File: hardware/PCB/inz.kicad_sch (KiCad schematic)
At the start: 24 parts, among them J1 Conn_01x20_Socket, J10 WCS1800, J11 INA333, J12 Micro SD Adapter, J13 Relays, J2 Conn_01x20_Socket, J3 USB_C_Receptacle_USB2.0_16P, J4 Barrel_Jack_Switch, J5 J_OLED, J6 J_SGP30, J7 J_BMP1, J8 J_BMP2, J9 J_BMP3, U1 LM2596S-ADJ, U3 USBLC6-2SC6

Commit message: pcb
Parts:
- removed J10: WCS1800, Connector_PinHeader_2.54mm:PinHeader_1x04_P2.54mm_Vertical, symbol Connector:Conn_01x04_Pin
- removed J11: INA333, Connector_PinHeader_2.54mm:PinHeader_1x04_P2.54mm_Vertical, symbol Connector:Conn_01x04_Pin
- removed J12: Micro SD Adapter, Connector_PinHeader_2.54mm:PinHeader_1x06_P2.54mm_Vertical, symbol Connector:Conn_01x06_Pin
- removed J13: Relays, Connector_PinHeader_2.54mm:PinHeader_1x06_P2.54mm_Vertical, symbol Connector:Conn_01x06_Pin
- removed J4: Barrel_Jack_Switch, Connector_BarrelJack:BarrelJack_Horizontal, symbol Connector:Barrel_Jack_Switch
- added C104, C105, C106: 100n, Capacitor_SMD:C_0805_2012Metric, symbol Device:C
- added D101: D_Schottky, Diode_SMD:D_SMA, symbol Device:D_Schottky
- added F201: 2A, Fuse:Fuseholder_Clip-5x20mm_Littelfuse_111_Inline_P20.00x5.00mm_D1.05mm_Horizontal, symbol Device:Polyfuse
- added J102: Conn_01x02, symbol Connector_Generic:Conn_01x02
- added J103: enc, Connector_PinHeader_2.54mm:PinHeader_1x05_P2.54mm_Vertical, symbol Connector:Conn_01x05_Pin
- added R104, R105, R106: 5.1k, Resistor_SMD:R_0805_2012Metric, symbol Device:R
- added SW101: RotaryEncoder_Switch_MP, symbol Device:RotaryEncoder_Switch_MP
- J5: now left out of the parts list
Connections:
- net 5V is gone; now on net +5V: J1.18 (Pin_18)
- net +3V3: now also J103.1 (Pin_1); no longer J1.20 (Pin_20), J2.3 (Pin_3)
- net BMP1_CS: no longer J1.11 (Pin_11), J2.11 (Pin_11), J8.5 (Pin_5)
- net GND: now also C104.2, C105.2, C106.2, J103.5 (Pin_5), SW101.S2
- net +5V: now reaches Cin.1, U1.1 (VIN)
- net +5V: now also J2.1 (Pin_1)
- net B0 renamed QNH_out_B0
- net B1 renamed ina333_Vout_B1
- net VUSB: no longer names the net of J3.A4 (VBUS), J3.A9 (VBUS), J3.B4 (VBUS), J3.B9 (VBUS), U3.5 (VBUS)
- new net 3V3: J1.20 (Pin_20), J2.3 (Pin_3)
- new net B3: J1.11 (Pin_11), J8.5 (Pin_5)
- new net SD_CS: J2.11 (Pin_11)
- new net Sensors1/ina333_Vin+: J102.1 (Pin_1)
- new net Sensors1/ina333_Vin-: J102.2 (Pin_2)
- new net enc_KEY: C106.1, R106.2
- new net enc_S1: C104.1, R104.2
- new net enc_S1_in: J103.4 (Pin_4), R104.1
- new net enc_S2: C105.1, R105.2
- new net enc_S2_in: J103.3 (Pin_3), R105.1
- new net enc_key_in: J103.2 (Pin_2), R106.1, SW101.S1
- no-connect marks 9 -> 3
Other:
- added sheet Sensors1 (Sensors1.kicad_sch)
- note added: "Botland footprint"
- note added: "D"
- note added: "JST-XH 2.5mm"
- note added: "VCC GND SCK MOSI CS MISO"
- note added: "dupont 2.54mm"
- note added: "globalne na lokalne"
- note added: "kolejnosc"
- note added: "to ja zrobie"
- note added: "to zmienic na 2.8 pinout"
- note added: "wszędzie maja byc miejsca na zamontowanie przewodów zewnetrznych BMS TP4056 - footprint"
- note removed: "Tutaj chyba mial byc jakis modul na obudowe do wsadzania a reszta jakies rezystorki cos to na pcb?"
- note removed: "chyba sie zesra jak 3.3v i 5v na raz podlacze?"
- moved on the sheet: J1, J2, J3, J5, J6, J7, J8, J9, R3, R4, U3

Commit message: pcb commit
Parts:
- removed J5: J_OLED, Connector_PinHeader_2.54mm:PinHeader_1x08_P2.54mm_Vertical, symbol Connector:Conn_01x08_Pin
- removed J6: J_SGP30, Connector_PinHeader_2.54mm:PinHeader_1x05_P2.54mm_Vertical, symbol Connector:Conn_01x05_Pin
- added C2: 10u, Capacitor_SMD:C_0805_2012Metric, symbol Device:C
- added J4: J_OLED, Connector_PinHeader_2.54mm:PinHeader_1x14_P2.54mm_Vertical, symbol Connector:Conn_01x14_Pin
- added J5: J_SGP30, symbol Connector:Conn_01x04_Pin
- added J_BAT1: Conn_01x02, TerminalBlock:TerminalBlock_MaiXu_MX126-5.0-02P_1x02_P5.00mm, symbol Connector_Generic:Conn_01x02
- added Q2: IRLZ44N, Package_TO_SOT_THT:TO-220-3_Vertical, symbol Transistor_FET:IRLZ44N
- added R5: 1k, Resistor_SMD:R_0805_2012Metric, symbol Device:R
- added R6: 1, Resistor_SMD:R_0805_2012Metric, symbol Device:R
- added U4: LM358, footprints:LM358, symbol Amplifier_Operational:LM358
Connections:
- net +3V3: now also J4.1 (Pin_1), J4.8 (Pin_8), J5.1 (Pin_1)
- net +5V: now also U4.8 (V+)
- net GND: now also C2.2, J4.2 (Pin_2), J5.2 (Pin_2), J_BAT1.2 (Pin_2), R6.1, U4.4 (V-)
- net B3 renamed BMP2_CS
- net BMP2_CS: no longer J1.11 (Pin_11)
- net B4 renamed TIM3_CH1_PWM_B4
- net TIM3_CH1_PWM_B4: now also R5.1
- removed net BMP1_CS: J1.13 (Pin_13), J1.16 (Pin_16), J2.14 (Pin_14), J7.5 (Pin_5), J9.5 (Pin_5)
- net I2C_SCL renamed I2C_SCL_B6
- net I2C_SCL_B6: now also J5.3 (Pin_3)
- net I2C_SDA renamed I2C_SDA_B9
- net I2C_SDA_B9: now also J5.4 (Pin_4)
- net OLED_DC renamed OLED_DC_A2
- net OLED_DC_A2: now also J4.5 (Pin_5)
- net OLED_RST renamed OLED_RST_A3
- net OLED_RST_A3: now also J4.4 (Pin_4)
- net R1IN1 renamed R1_IN1_B12
- net R1IN2 renamed R1_IN2_B13
- net R1IN3 renamed R1_IN3_B14
- net SD_CS renamed SD_CS_A4
- net SPI_MISO renamed SPI_MISO_A6
- net SPI_MISO_A6: now also J4.9 (Pin_9)
- net SPI_MOSI renamed SPI_MOSI_A7
- net SPI_MOSI_A7: now also J4.6 (Pin_6)
- net SPI_SCK renamed SPI_SCK_A5
- net SPI_SCK_A5: now also J4.7 (Pin_7)
- net USB_D+ renamed USB_D+_A12
- net USB_D- renamed USB_D-_A11
- new net: C2.1, R5.2, U4.3 (+)
- new net: J_BAT1.1 (Pin_1), Q2.2 (D)
- new net: Q2.1 (G), U4.1
- new net: Q2.3 (S), R6.2, U4.2 (-)
- new net BMP1_CS_B5: J1.13 (Pin_13), J7.5 (Pin_5)
- new net BMP2_CS_B3: J1.11 (Pin_11)
- new net BMP3_CS_B8: J1.16 (Pin_16), J9.5 (Pin_5)
- new net OLED_CS_A1: J2.14 (Pin_14), J4.3 (Pin_3)
- no-connect marks 3 -> 7
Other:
- note added: "Bat+"
- note added: "Bat-"
- note added: "VCC GND CS RESET DC/RS SDI(MOSI) SCK LED SDO(MISO) T_CLK T_CS T_DIN T_DO T_IRQ"
- note added: "VCC GND SCL SDA"
- note added: "https://piotr-gorecki.pl/yk012-wspolnie-projektujemy-uniwersalne-obciazenie-aktywne/"
- note added: "lm358 irlz44n 10uF R = 1kohm ? Rs = 1ohm"
- note removed: "globalne na lokalne"
- note removed: "kolejnosc"
- note removed: "to zmienic na 2.8 pinout"
- moved on the sheet: C104, C105, C106, J103, J3, R104, R105, R106, R3, R4, SW101, U3

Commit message: PCB
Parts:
- removed C2: 10u, Capacitor_SMD:C_0805_2012Metric, symbol Device:C
- removed Cf: 2.2n, Capacitor_SMD:C_0805_2012Metric, symbol Device:C
- removed Cin: 150uF, Capacitor_SMD:CP_Elec_8x10.5, symbol Device:C_Polarized
- removed Cout: 680uF, Capacitor_SMD:CP_Elec_16x17.5, symbol Device:C_Polarized
- removed D1: 650mV 3A, Diode_SMD:D_SMA, symbol Device:D_Schottky
- removed J4: J_OLED, Connector_PinHeader_2.54mm:PinHeader_1x14_P2.54mm_Vertical, symbol Connector:Conn_01x14_Pin
- removed J5: J_SGP30, symbol Connector:Conn_01x04_Pin
- removed J7: J_BMP1, Connector_PinHeader_2.54mm:PinHeader_1x06_P2.54mm_Vertical, symbol Connector:Conn_01x06_Pin
- removed J8: J_BMP2, Connector_PinHeader_2.54mm:PinHeader_1x06_P2.54mm_Vertical, symbol Connector:Conn_01x06_Pin
- removed J9: J_BMP3, Connector_PinHeader_2.54mm:PinHeader_1x06_P2.54mm_Vertical, symbol Connector:Conn_01x06_Pin
- removed J_BAT1: Conn_01x02, TerminalBlock:TerminalBlock_MaiXu_MX126-5.0-02P_1x02_P5.00mm, symbol Connector_Generic:Conn_01x02
- removed L1: 39uH, Inductor_SMD:L_12x12mm_H8mm, symbol Device:L
- removed Q2: IRLZ44N, Package_TO_SOT_THT:TO-220-3_Vertical, symbol Transistor_FET:IRLZ44N
- removed R5: 1k, Resistor_SMD:R_0805_2012Metric, symbol Device:R
- removed R6: 1, Resistor_SMD:R_0805_2012Metric, symbol Device:R
- removed Rfb1: 3.3k, Resistor_SMD:R_0805_2012Metric, symbol Device:R
- removed Rfb2: 5.6k, Resistor_SMD:R_0805_2012Metric, symbol Device:R
- removed U1: LM2596S-ADJ, Package_TO_SOT_SMD:TO-263-5_TabPin3, symbol Regulator_Switching:LM2596S-ADJ
- removed U4: LM358, footprints:LM358, symbol Amplifier_Operational:LM358
- added C107, C109, C110: 100n, Capacitor_SMD:C_0805_2012Metric, symbol Device:C
- added C108: 2.2u, Capacitor_SMD:C_0805_2012Metric, symbol Device:C
- added L101: 2.2uH, Inductor_SMD:L_Sunlord_MWSA0503S, symbol Device:L
- added R107: 100k, Resistor_SMD:R_0805_2012Metric, symbol Device:R
- added R108: 22.1k, Resistor_SMD:R_0805_2012Metric, symbol Device:R
- added U101: LMR51430, Package_TO_SOT_SMD:SOT-23-6, symbol Regulator_Switching:LMR51430
- C104, C105, C106: Distributor https://jlcpcb.com/partdetail/28983-CL21B104KCFNNNE/C28233 -> (none); JLCPCB Part (none) -> C28233; Link (none) -> https://jlcpcb.com/partdetail/28983-CL21B104KCFNNNE/C28233
- D101: value D_Schottky -> D_Schottky_3A; Distributor https://jlcpcb.com/partdetail/MDD_Microdiode_Semiconductor-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 -> (none); JLCPCB Part (none) -> C8678; Link (none) -> https://jlcpcb.com/partdetail/MDD_Microdiode_Semiconductor-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
- F201: value 2A -> xA; Distributor https://jlcpcb.com/partdetail/XuchengElec-5x20/C3130 -> (none); Link (none) -> https://jlcpcb.com/partdetail/XuchengElec-5x20/C3130; MFR Part 5x20 环保 保险管夹/座 -> (none); Manufacturer Xucheng Elec -> (none); now left out of the parts list
- J102: value Conn_01x02 -> ina333; footprint (none) -> TerminalBlock:TerminalBlock_MaiXu_MX126-5.0-02P_1x02_P5.00mm
- J103: JLCPCB Part (none) -> C2337; LCSC C2337 -> (none)
- J3: Link (none) -> https://jlcpcb.com/partdetail/3554049-USB4105_GF_A060/C3025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; Link 1 https://jlcpcb.com/partdetail/3554049-USB4105_GF_A060/C3025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 -> (none)
- R104, R105, R106: Distributor https://jlcpcb.com/partdetail/28584-0805W8F5101T5E/C27834 -> (none); Link (none) -> https://jlcpcb.com/partdetail/28584-0805W8F5101T5E/C27834
- R3, R4: footprint (none) -> Resistor_SMD:R_0805_2012Metric; Link (none) -> https://jlcpcb.com/partdetail/28584-0805W8F5101T5E/C27834; MFR Part (none) -> 0805W8F5101T5E; Manufacturer (none) -> UNI-ROYAL(Uniroyal Elec)
- U3: Likn 1 https://jlcpcb.com/partdetail/STMicroelectronics-USBLC62SC6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 -> (none); Link (none) -> https://jlcpcb.com/partdetail/STMicroelectronics-USBLC62SC6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
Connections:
- net +5V is gone; now on net VBUS: J1.18 (Pin_18), J2.1 (Pin_1)
- net +3V3: now also C110.2, L101.2, R107.1
- net GND: now also C108.2, C109.2, C110.1, R108.2, U101.1 (GND)
- net at D101.1 (K): now also F201.1
- net VBUS: now reaches D101.2 (A)
- net at F201.2: now also C108.1, C109.1, U101.3 (VIN), U101.5 (EN)
- new net: C107.1, L101.1, U101.2 (SW)
- new net: R107.2, R108.1, U101.4 (FB)
- new net: C107.2, U101.6 (CB)
- no-connect marks 7 -> 2
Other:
- added sheet Connectors (Connectors.kicad_sch)
- added sheet Sensors2 (Sensors2.kicad_sch)
- sheet Sensors1 ports: added pwm_current_sel; removed none
- note added: "5.0V -> 3.3V"
- note removed: "Bat+"
- note removed: "Bat-"
- note removed: "D"
- note removed: "JST-XH 2.5mm"
- note removed: "VCC GND CS RESET DC/RS SDI(MOSI) SCK LED SDO(MISO) T_CLK T_CS T_DIN T_DO T_IRQ"
- note removed: "VCC GND SCK MOSI CS MISO"
- note removed: "VCC GND SCL SDA"
- note removed: "dupont 2.54mm"
- note removed: "https://piotr-gorecki.pl/yk012-wspolnie-projektujemy-uniwersalne-obciazenie-aktywne/"
- note removed: "lm358 irlz44n 10uF R = 1kohm ? Rs = 1ohm"
- note removed: "to ja zrobie"
- moved on the sheet: D101, F201

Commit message: PCB
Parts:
- removed J1, J2: Conn_01x20_Socket, symbol Connector:Conn_01x20_Socket
- removed SW101: RotaryEncoder_Switch_MP, symbol Device:RotaryEncoder_Switch_MP
- added J15: STM32blackpill, footprints:STM32blackpill, symbol footprints:STM32blackpill
- added JP2: SolderJumper_2_Open, Jumper:SolderJumper-2_P1.3mm_Open_TrianglePad1.0x1.5mm, symbol Jumper:SolderJumper_2_Open
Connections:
- net GND: now also J15.19 (GND), J15.22 (GND)
- net +5V: now reaches C108.1, C109.1, F201.2, U101.3 (VIN), U101.5 (EN)
- net +5V: now also J15.18 (5V), J15.21 (5V)
- net USB_D+_A12 renamed USB_D+
- net USB_D+: now also J15.9 (PA12)
- net USB_D-_A11 renamed USB_D-
- net USB_D-: now also J15.8 (PA11)
- new net BMP1_CS: J15.13 (PB5)
- new net BMP2_CS: J15.11 (PB3)
- new net BMP3_CS: J15.16 (PB8)
- new net I2C_SCL: J15.14 (PB6)
- new net I2C_SDA: J15.17 (PB9)
- new net OLED_CS: J15.34 (PA1)
- new net OLED_DC: J15.33 (PA2)
- new net OLED_RST: J15.32 (PA3)
- new net QNH_out: J15.27 (PB0)
- new net R1_IN1: J15.1 (PB12)
- new net R1_IN2: J15.2 (PB13)
- new net R1_IN3: J15.3 (PB14)
- new net SD_CS: J15.31 (PA4)
- new net SPI_MISO: J15.29 (PA6)
- new net SPI_MOSI: J15.28 (PA7)
- new net SPI_SCK: J15.30 (PA5)
- new net Sensors1/Current_sensor_in+: JP2.1 (A)
- new net Sensors1/Current_sensor_in-: JP2.2 (B)
- new net TIM3_CH1_PWM: J15.12 (PB4)
- new net ina333_Vout: J15.26 (PB1)
- no-connect marks 2 -> 5
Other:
- sheet Sensors1 ports: added BME280_SPI_CLK, BME280_SPI_MISO, BME282_SPI_MOSI, BME283_SPI_CS, Current_sensor_in+, Current_sensor_in-; removed pwm_current_sel
- sheet Sensors2 ports: added pwm_current_sel; removed none
- note removed: "Botland footprint"
- moved on the sheet: J102

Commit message: pcb sensors
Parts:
- removed C104, C105, C106, C107, C109, C110: 100n, Capacitor_SMD:C_0805_2012Metric, symbol Device:C
- removed C108: 2.2u, Capacitor_SMD:C_0805_2012Metric, symbol Device:C
- removed D101: D_Schottky_3A, Diode_SMD:D_SMA, symbol Device:D_Schottky
- removed F201: xA, Fuse:Fuseholder_Clip-5x20mm_Littelfuse_111_Inline_P20.00x5.00mm_D1.05mm_Horizontal, symbol Device:Polyfuse
- removed J102: ina333, TerminalBlock:TerminalBlock_MaiXu_MX126-5.0-02P_1x02_P5.00mm, symbol Connector_Generic:Conn_01x02
- removed J103: enc, Connector_PinHeader_2.54mm:PinHeader_1x05_P2.54mm_Vertical, symbol Connector:Conn_01x05_Pin
- removed J3: USB_C_Receptacle_USB2.0_16P, Connector_USB:USB_C_Receptacle_GCT_USB4105-xx-A_16P_TopMnt_Horizontal, symbol Connector:USB_C_Receptacle_USB2.0_16P
- removed L101: 2.2uH, Inductor_SMD:L_Sunlord_MWSA0503S, symbol Device:L
- removed R104, R105, R106, R3, R4: 5.1k, Resistor_SMD:R_0805_2012Metric, symbol Device:R
- removed R107: 100k, Resistor_SMD:R_0805_2012Metric, symbol Device:R
- removed R108: 22.1k, Resistor_SMD:R_0805_2012Metric, symbol Device:R
- removed U101: LMR51430, Package_TO_SOT_SMD:SOT-23-6, symbol Regulator_Switching:LMR51430
- removed U3: USBLC6-2SC6, Package_TO_SOT_SMD:SOT-23-6, symbol Power_Protection:USBLC6-2SC6
- added J101: battery cell, symbol Connector:Screw_Terminal_01x02
- added U105: TP4056, symbol footprints:TP4056
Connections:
- net GND: now also U105.2 (GND), U105.6 (OUT-)
- net enc_KEY: now also J15.7 (PA10)
- net enc_S1: now also J15.5 (PA8)
- net enc_S2: now also J15.6 (PA9)
- net Sensors1/Current_sensor_in+ renamed Current_sensor_in+
- net Current_sensor_in+: now also J101.2 (Pin_2)
- net Sensors1/Current_sensor_in- renamed Current_sensor_in-
- net Current_sensor_in-: now also U105.4 (BAT+)
- new net K1_NO: U105.1 (Vusb)
- new net K2_COM: U105.3 (OUT+)
- new net ina333_Vin-: J101.1 (Pin_1), U105.5 (BAT-)
- no-connect marks 5 -> 3
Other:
- added sheet Relays (Relays.kicad_sch)
- sheet Connectors ports: added BMP1_CS, BMP2_CS, I2C_SCL, I2C_SDA, OLED_CS, OLED_DC, OLED_RST, SPI_MISO, SPI_MOSI, SPI_SCK, enc_KEY, enc_S1, enc_S2; removed none
- sheet Sensors1 ports: added none; removed BME280_SPI_CLK, BME280_SPI_MISO, BME282_SPI_MOSI, BME283_SPI_CS
- sheet Sensors2 ports: added BMP3_CS, Bat_load+, Bat_load-, SD_CS, SPI_MISO, SPI_MOSI, SPI_SCK; removed none
- note removed: "5.0V -> 3.3V"
- moved on the sheet: J15A, J15B, JP2

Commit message: Rough Layout pcb
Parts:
- added TP101, TP102, TP103, TP104, TP105, TP106, TP107, TP108, TP109, TP110, TP111: TestPoint, TestPoint:TestPoint_Pad_D1.5mm, symbol Connector:TestPoint
- J101: renamed from U105; footprint (none) -> footprints:board_TP4056; Link (none) -> https://pl.aliexpress.com/item/1005010441916443.html?spm=a2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
- J102: renamed from J101; value battery cell -> Battery; footprint (none) -> TerminalBlock_Phoenix:TerminalBlock_Phoenix_MKDS-1,5-2_1x02_P5.00mm_Horizontal; now left out of the parts list
- J103: renamed from J15; Link (none) -> https://pl.aliexpress.com/item/1005001456186625.html?spm=a2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; now left out of the parts list
- renumbered JP2 to JP101
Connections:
- net OLED_CS: now also J103.10 (PA15)
- net at J103.23 (3V3): now also TP101.1
- net at J103.24 (PB10): now also TP103.1
- net at J103.25 (PB2): now also TP104.1
- net at J103.35 (PA0): now also TP105.1
- net at J103.36 (RST): now also TP106.1
- net at J103.37 (PC15): now also TP107.1
- net at J103.38 (PC14): now also TP108.1
- net at J103.39 (PC13): now also TP109.1
- net at J103.40 (VB): now also TP111.1
- net TIM4_CH2: now reaches J103.15 (PB7)
- net at J103.20 (3V3): now also TP110.1
- net at J103.4 (PB15): now also TP102.1
- net QNH_out renamed QNH_Vout
- no-connect marks 3 -> 0
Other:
- sheet Connectors ports: added OLED_TIM2, SD_CS; removed none
- sheet Sensors1 ports: added QNH_Vout; removed QNH_out
- sheet Sensors2 ports: added none; removed SD_CS
- note removed: "wszędzie maja byc miejsca na zamontowanie przewodów zewnetrznych BMS TP4056 - footprint"
- moved on the sheet: J103A, J103B

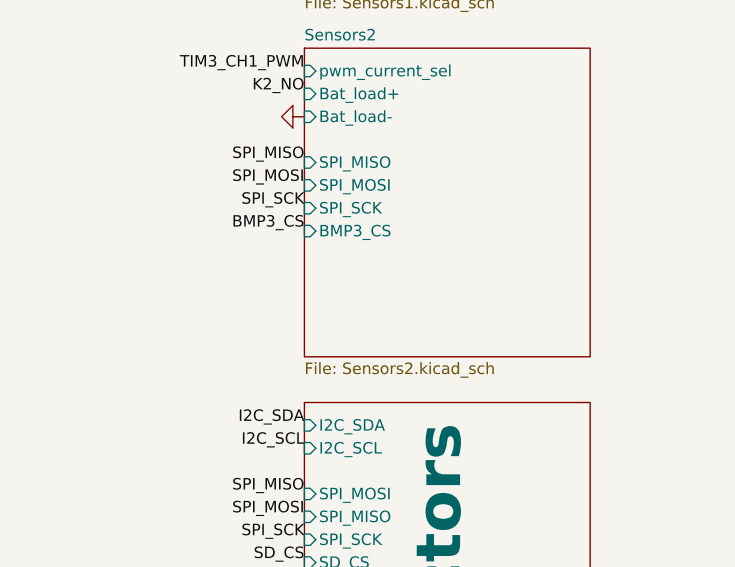
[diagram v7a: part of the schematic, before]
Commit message: pcb XL4015
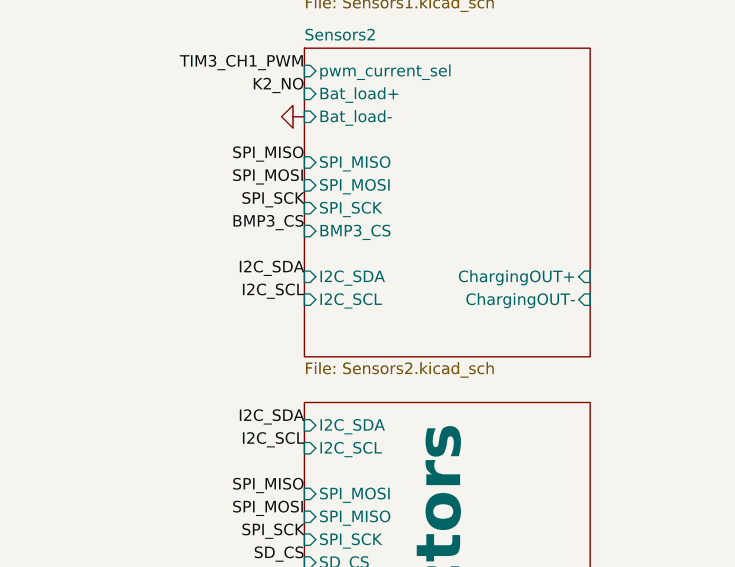
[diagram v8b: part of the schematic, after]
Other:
- sheet Sensors2 ports: added ChargingOUT+, ChargingOUT-, I2C_SCL, I2C_SDA; removed none
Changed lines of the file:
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@@
+		)
+	)
+	(label "I2C_SDA"
+		(at 240.03 78.74 180)
+		(effects
+			(font
+				(size 1.27 1.27)
+			)
+			(justify right bottom)
 		)
 	)
@@
 	(label "Current_sensor_in+"
 		(at 240.03 27.94 180)
+		(effects
+			(font
+				(size 1.27 1.27)
+			)
+			(justify right bottom)
+		)
+	)
+	(label "I2C_SCL"
+		(at 240.03 81.28 180)
 		(effects
 			(font
@@
 			)
 		)
+		(pin "I2C_SCL" input
+			(at 240.03 81.28 180)
+			(effects
+				(font
+					(size 1.27 1.27)
+				)
+				(justify left)
+			)
+		)
+		(pin "I2C_SDA" input
+			(at 240.03 78.74 180)
+			(effects
+				(font
+					(size 1.27 1.27)
+				)
+				(justify left)
+			)
+		)
+		(pin "ChargingOUT-" input
+			(at 271.78 81.28 0)
+			(effects
+				(font
+					(size 1.27 1.27)
+				)
+				(justify right)
+			)
+		)
+		(pin "ChargingOUT+" input
+			(at 271.78 78.74 0)
+			(effects
+				(font
+					(size 1.27 1.27)
+				)
+				(justify right)
+			)
+		)
